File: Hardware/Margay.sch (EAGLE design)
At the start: 70 parts, among them IC1 ATMEGA644M, J1 CONN_42.54_SCREW, J2 CONN_6SCREW_2.54, Q1 FDN360P, Q2 DMG3404, Q3 2N7002, Q4 FDN360P, Q6 FDN360P, U2 FT231X-Q

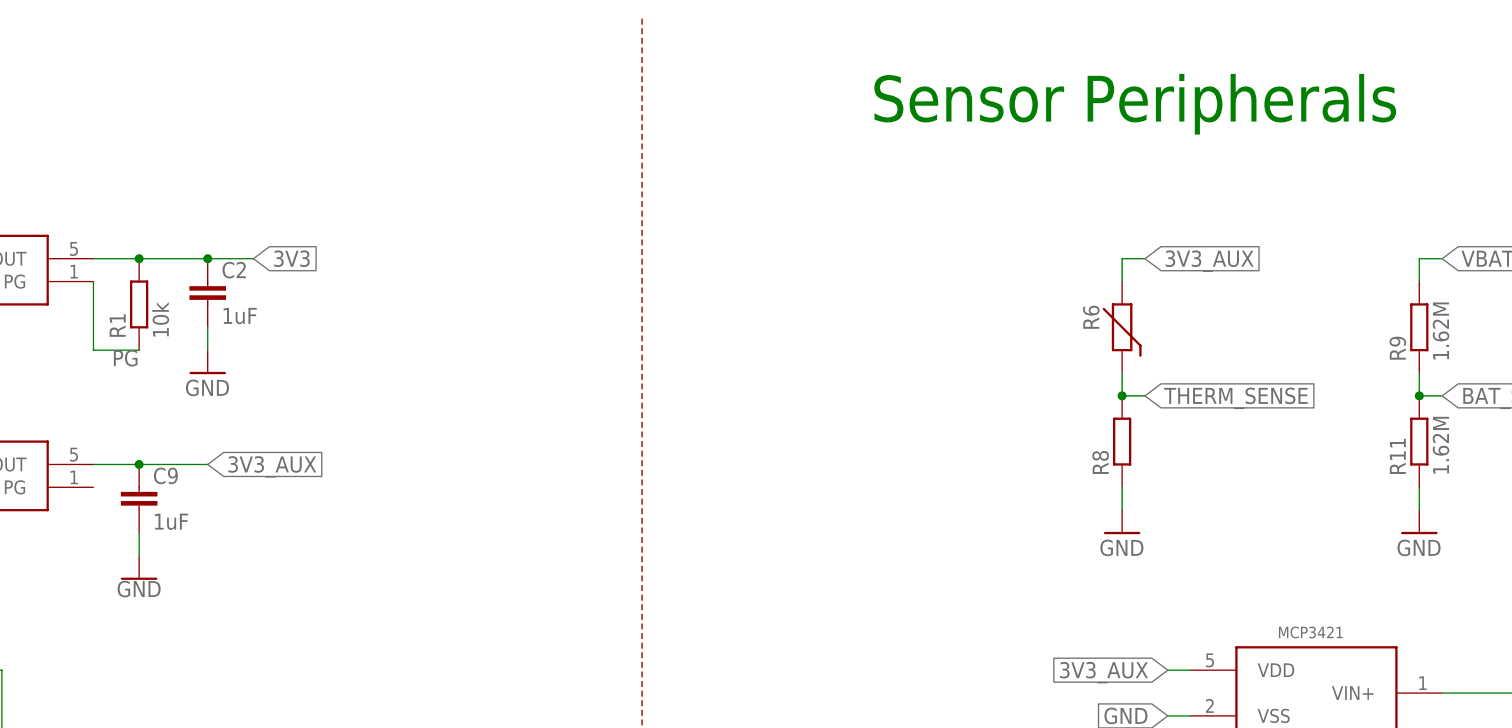
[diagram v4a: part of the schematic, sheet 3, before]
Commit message: First round of v2 updates to schematic
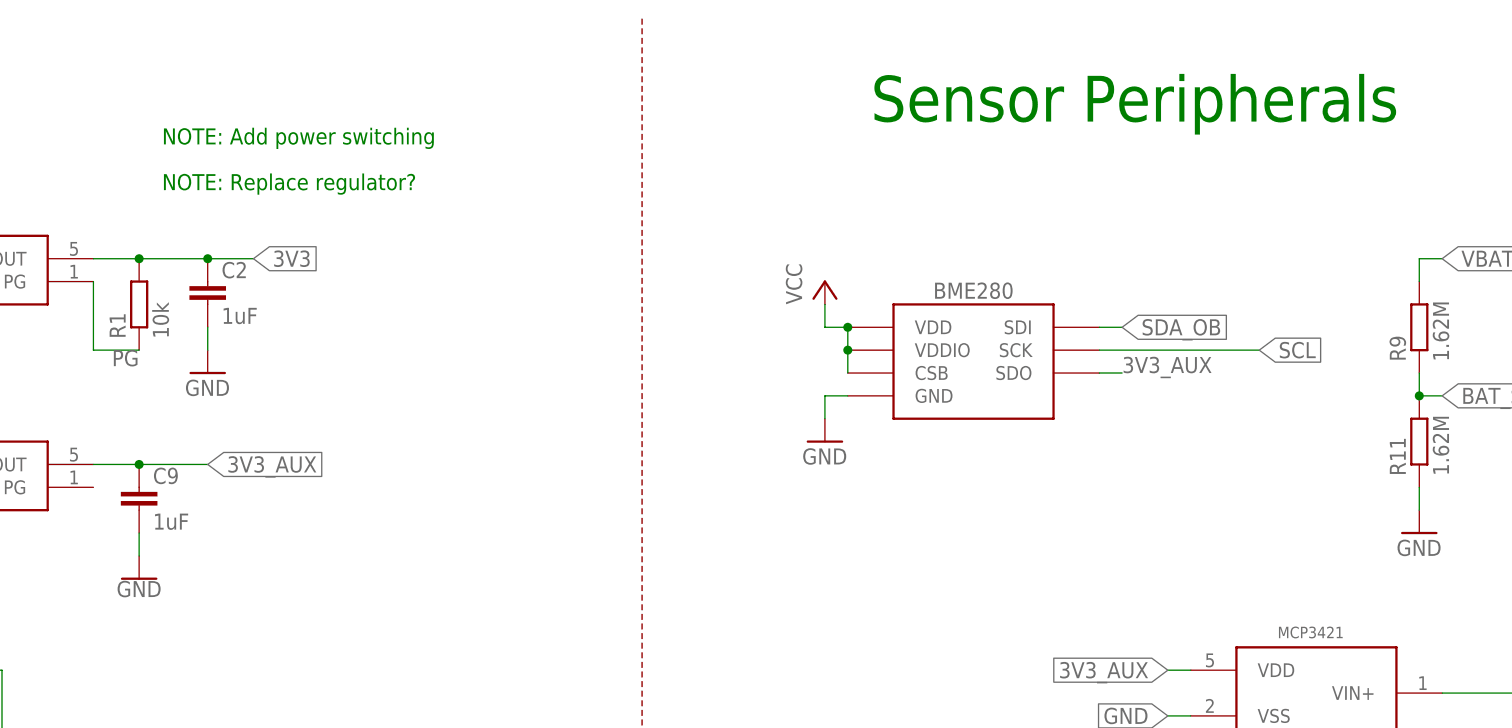
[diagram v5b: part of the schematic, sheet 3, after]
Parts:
- removed R6: (no value), bschulz:THERMISTOR10K
- removed R8: (no value), bschulz_passives:R-EU_P10KR0603
- added R18, R19: 4.7k, bschulz_passives:R-EU_R0402
- added U$12: BME280, bschulz:BME280
- C1, C14, C17, C3, C4, C6, C7, C8: device bschulz_passives:C-EU0.1UFC0603 -> bschulz_passives:C-EU0.1UFC0402
- C21: device bschulz_passives:C-EU1UFC0603 -> bschulz_passives:C-EU0.1UFC0402
- R13, R3: device bschulz:R-EU_10KR0603 -> bschulz_passives:R-EU_10KR0402
- R15: device bschulz_passives:R-EU_10KR0603 -> bschulz_passives:R-EU_R0402
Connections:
- new net ADC_EXT: IC1.(PCINT3/ADC3)PA3, J2.5
- new net RX_EXT: IC1.(PCINT26/INT0)PD2, J2.4
- new net TX_EXT: IC1.(PCINT27/INT1)PD3, J2.3
- net 3V3_AUX: now also R18.2, R19.2, U$12.CSB, U$12.SDO, U$12.VDD, U$12.VDDIO; no longer R6.1
- net EXT_INT: no longer IC1.(PCINT27/INT1)PD3
- net GND: now also U$12.GND; no longer R8.1
- net LOG_INT: now also IC1.(PCINT4/ADC4)PA4; no longer IC1.(PCINT10/INT2/AIN0)PB2
- net MISO: no longer J2.4
- net MOSI_BUF: no longer J2.3
- net RTC_INT: now also IC1.(PCINT10/INT2/AIN0)PB2; no longer IC1.(PCINT26/INT0)PD2
- net SCK_BUF: no longer J2.5
- net SCL: now also R19.1, U$12.SCK
- net SDA: now also R18.1
- net SDA_OB: now also U$12.SDI
- net THERM_SENSE: no longer R6.2, R8.2
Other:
- note added: "Ext Int0"
- note added: "Ext Int1"
- note added: "I2C pullup to switched 3v3"
- note added: "NOTE: Add power switching"
- note added: "NOTE: Add voltage divider to ADC Ext??"
- note added: "NOTE: Check orientation of TX and RX"
- note added: "NOTE: Fix connector orientation on PCB!"
- note added: "NOTE: REDUCE RESISTOR SIZE"
- note added: "NOTE: Replace regulator?"
- note removed: "Jump auxillary power rails together, reduces brownout protection"

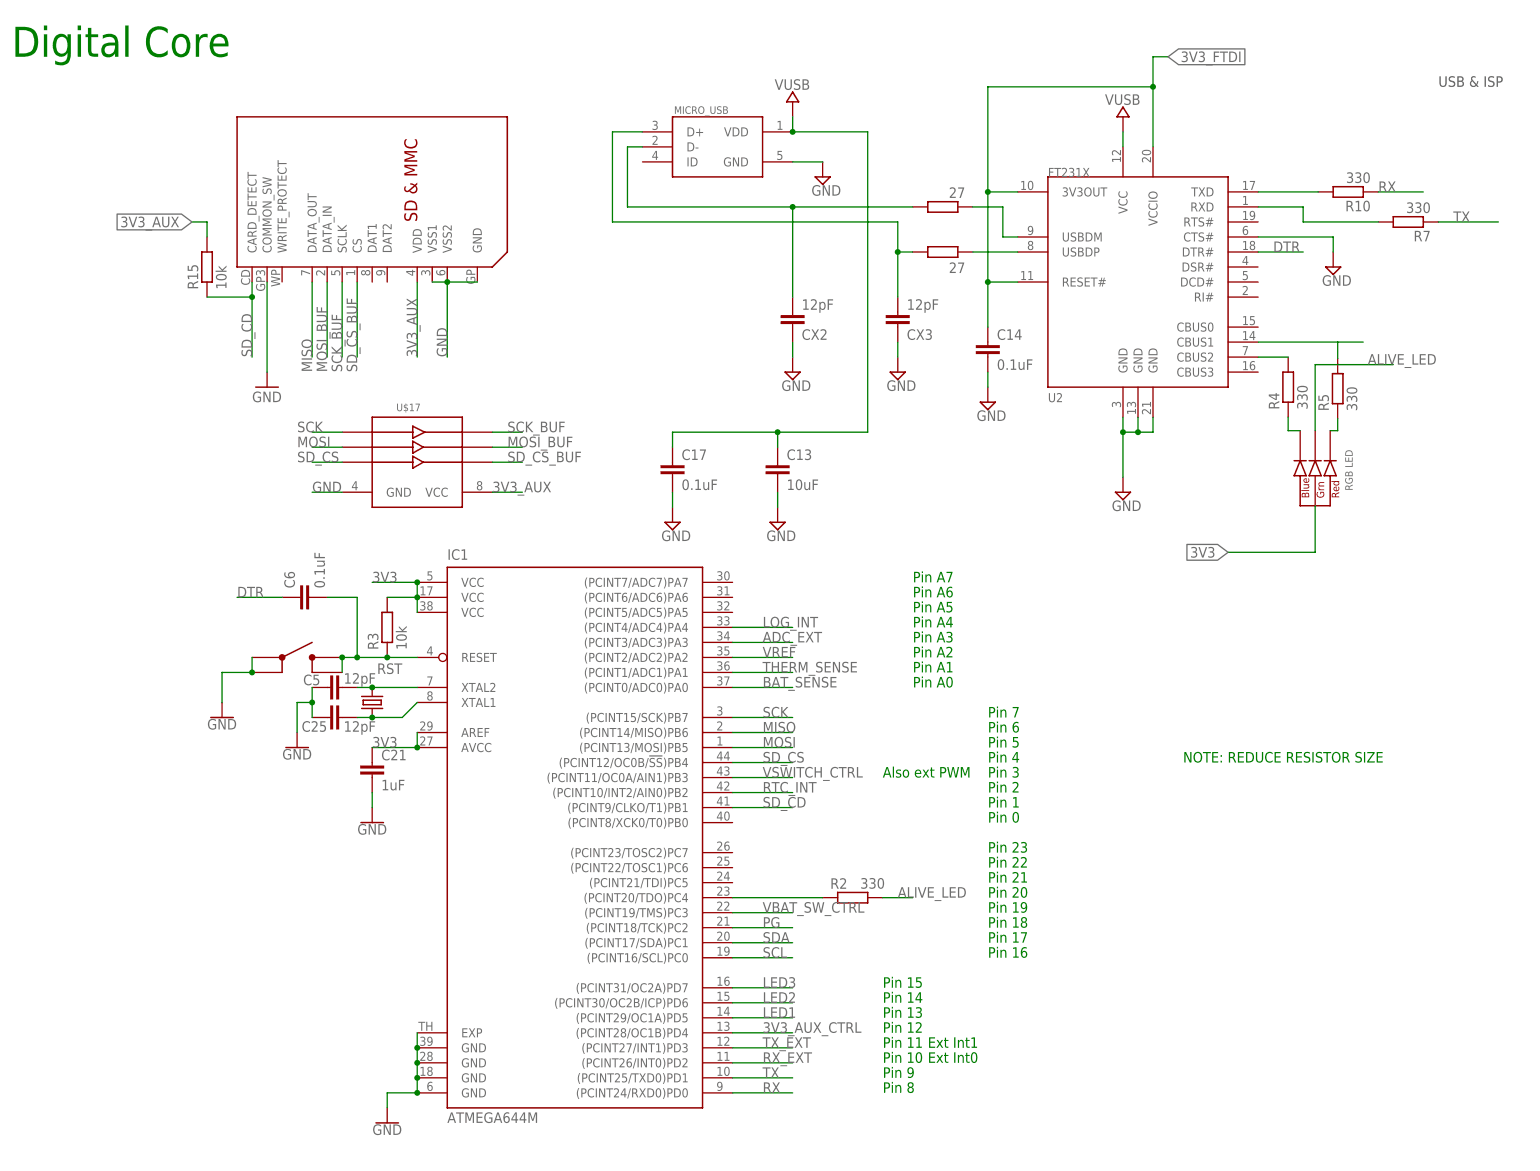
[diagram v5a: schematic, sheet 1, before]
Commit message: Revised schematic for Margay v2, added circuit simulations
Will remove some simulations later, still need to do much layout and placement, as well as verify the schematic
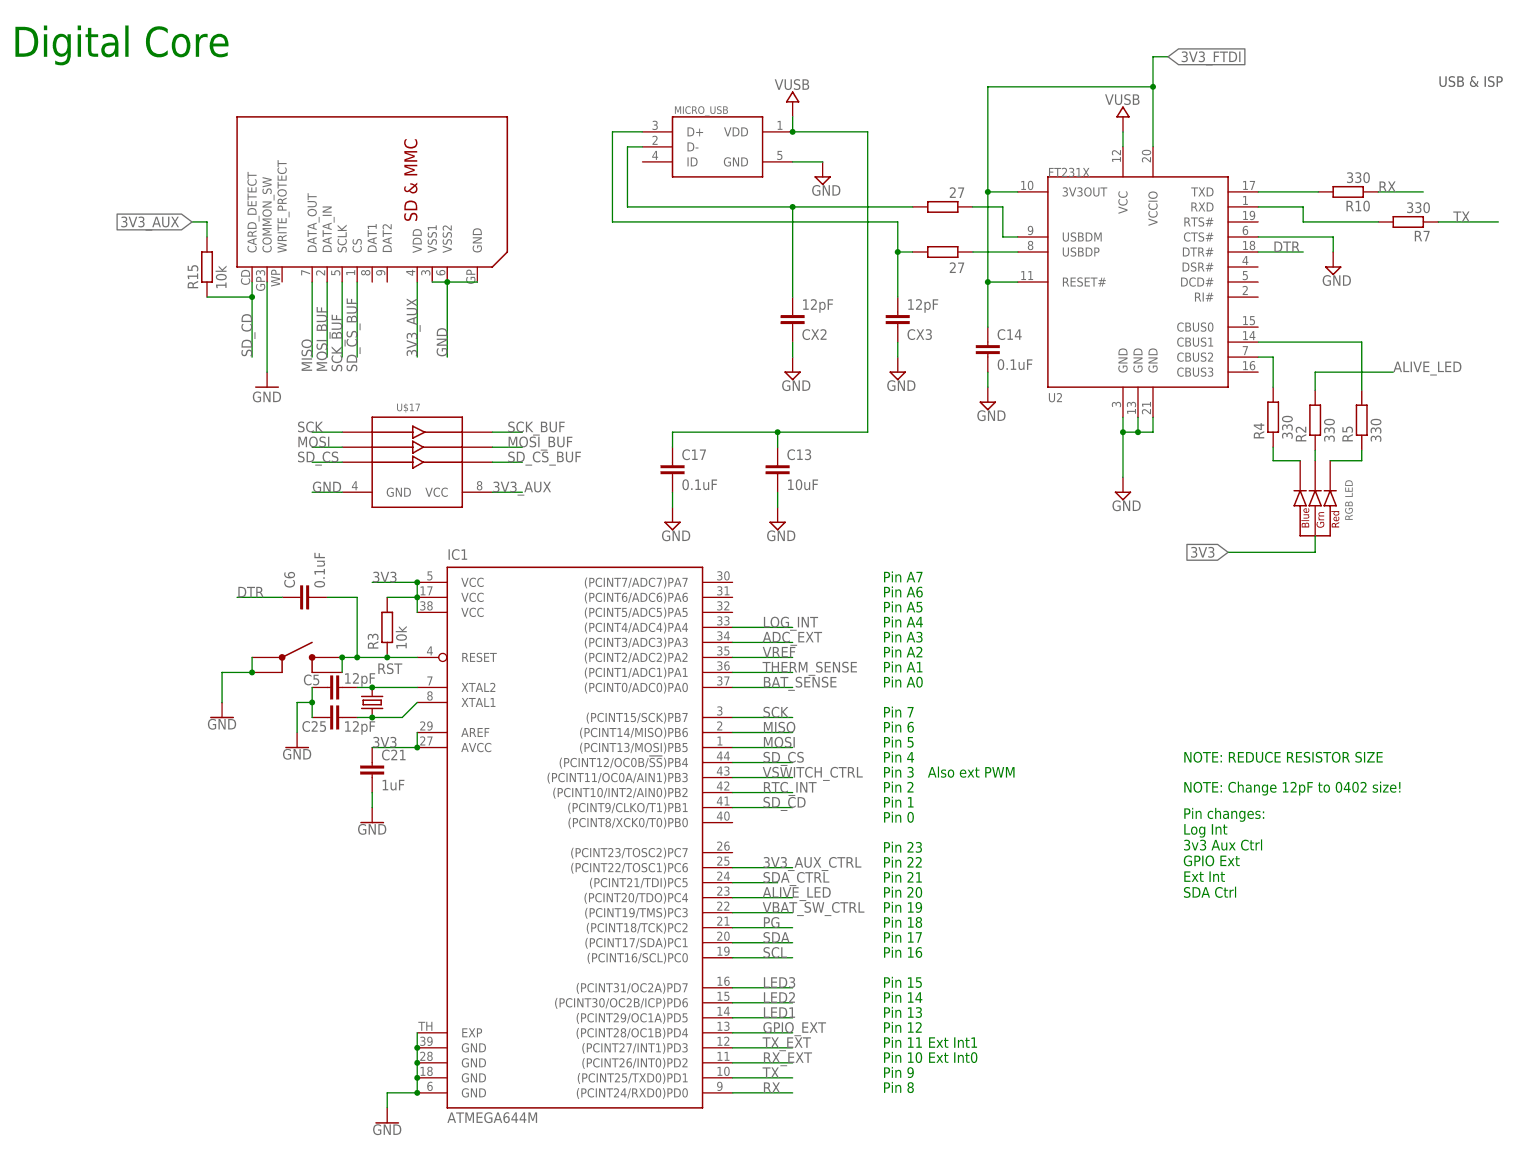
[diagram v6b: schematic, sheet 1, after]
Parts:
- removed Q6: FDN360P, bschulz:MOSFET_PCH-FDN360P
- removed U$10: TPS79733, bschulz:TPS79733
- removed U$11: MIC842H, bschulz:MIC842H
- added C10, C11: 0.1uF, bschulz_passives:C-EU0.1UFC0402
- added C12: 1uF, bschulz_passives:C-EU1UFC0603
- added U$18: TPS2105, bschulz:TPS2105
- added U1: TPS7A0533DBV, bschulz:TPS7A0533DBV
- C25, C5: device bschulz_passives:C-EUC0603 -> bschulz_passives:C-EU12PFC0402
- C7: value 0.1uF -> 1uF; device bschulz_passives:C-EU0.1UFC0402 -> bschulz_passives:C-EU1UFC0603
- C9: value 1uF -> 10uF; device bschulz_passives:C-EU1UFC0603 -> bschulz_passives:C-EU10UFC0805
- CX2, CX3: device bschulz_passives:C-EU12PFC0603 -> bschulz_passives:C-EU12PFC0402
- D+, D-: device bschulz_passives:R-EU_27R0603 -> bschulz_passives:R-EU_27R0402
- R1: device bschulz_passives:R-EU_10KR0603 -> bschulz_passives:R-EU_10KR0402
- R10, R4, R5, R7: device bschulz_passives:R-EU_330R0603 -> bschulz_passives:R-EU_330R0402
- R12: device bschulz_passives:R-EU_10KR0603 -> bschulz_passives:R-EU_P10KR0603
- R14, R23, R24: device bschulz:R-EU_330R0603 -> bschulz_passives:R-EU_330R0402
- R17: device bschulz_passives:R-EU_10KR0603 -> bschulz_passives:R-EU_330R0402
- R18, R19: device bschulz_passives:R-EU_R0402 -> bschulz_passives:R-EU_4.7KR0402
- R2: device bschulz:R-EU_330R0603 -> bschulz_passives:R-EU_330R0402; DIGIKEY (none) -> 311-330HRCT-ND; MPN (none) -> RC0603FR-07330RL
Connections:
- removed net EXT_INT: J2.6
- removed net N$4 (its old number): Q6.G, U$11.OUT
- new net GPIO_EXT: IC1.(PCINT28/OC1B)PD4, J2.6
- new net SDA_CTRL: IC1.(PCINT21/TDI)PC5, U$13.S
- net 3V3_AUX: now also U1.VOUT; no longer U$10.VOUT
- net 3V3_AUX_CTRL: now also IC1.(PCINT22/TOSC1)PC6, U1.EN; no longer IC1.(PCINT28/OC1B)PD4, U$13.S
- net ALIVE_LED: no longer U$16.GREEN_CATH
- net GND: now also C10.2, C11.2, C12.2, U$18.GND, U1.GND; no longer U$10.GND, U$11.GND
- net N$1: now also U$16.GREEN_CATH; no longer IC1.(PCINT20/TDO)PC4
- net VBAT+: now also C10.1, U$18.IN1; no longer Q6.S, U$11.VDD
- net VBAT_SW: now also C12.1, U$18.OUT, U1.VIN; no longer Q6.D, U$10.VIN
- net VBAT_SW_CTRL: now also U$18.EN; no longer U$11.INP
- net VUSB: now also C11.1, U$18.IN2
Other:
- note added: "NOTE: Add enable line connection??"
- note added: "NOTE: Add silkscreen note!"
- note added: "NOTE: Change 12pF to 0402 size!"
- note added: "NOTE: Reduce resistance?? Add capacitor in parellel"
- note added: "Pin changes: Log Int 3v3 Aux Ctrl GPIO Ext Ext Int SDA Ctrl"
- note removed: "NOTE: Replace regulator?"
- moved on the sheet: C9, R2, R4, R5

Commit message: Begining of v2 layout
Power section and severl problematic signals taken care of, still need to add BME280 and fix header connections
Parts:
- R17: device bschulz_passives:R-EU_330R0402 -> bschulz_passives:R-EU_10KR0402
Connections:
- net ALIVE_LED: now also IC1.(PCINT20/TDO)PC4
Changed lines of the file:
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@@
 <?xml version="1.0" encoding="utf-8"?>
 <!DOCTYPE eagle SYSTEM "eagle.dtd">
-<eagle version="9.0.1">
+<eagle version="9.1.3">
 <drawing>
 <settings>
@@
 <part name="Q4" library="bschulz" deviceset="MOSFET_PCH" device="-FDN360P" value="FDN360P"/>
 <part name="R16" library="bschulz_passives" deviceset="R-EU_" device="R0603" technology="180K" value="180k"/>
-<part name="R17" library="bschulz_passives" deviceset="R-EU_" device="R0402" technology="330" value="10k"/>
+<part name="R17" library="bschulz_passives" deviceset="R-EU_" device="R0402" technology="10K" value="10k"/>
 <part name="GND11" library="SparkFun-PowerSymbols" library_urn="urn:adsk.eagle:library:530" deviceset="GND" device=""/>
 <part name="C7" library="bschulz_passives" deviceset="C-EU" device="C0603" technology="1UF" value="1uF"/>
@@
 <wire x1="132.08" y1="58.42" x2="142.24" y2="58.42" width="0.1524" layer="91"/>
 <label x="137.16" y="58.42" size="1.778" layer="95"/>
-</segment>
-<segment>
+<pinref part="IC1" gate="G$1" pin="(PCINT20/TDO)PC4"/>
+</segment>
+<segment>

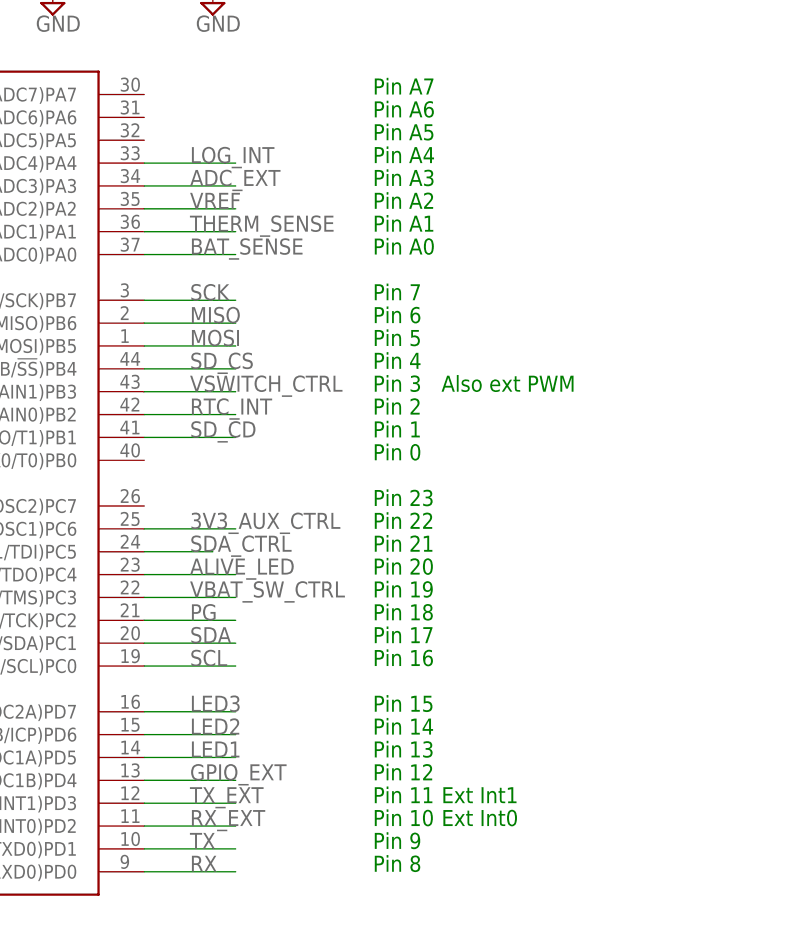
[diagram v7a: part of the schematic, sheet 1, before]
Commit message: Main v2 layout complete, needs review minor cleanup
Main layout is completed, needs verification and review for any traces which need to be cleaned up. Double check power on schematic!
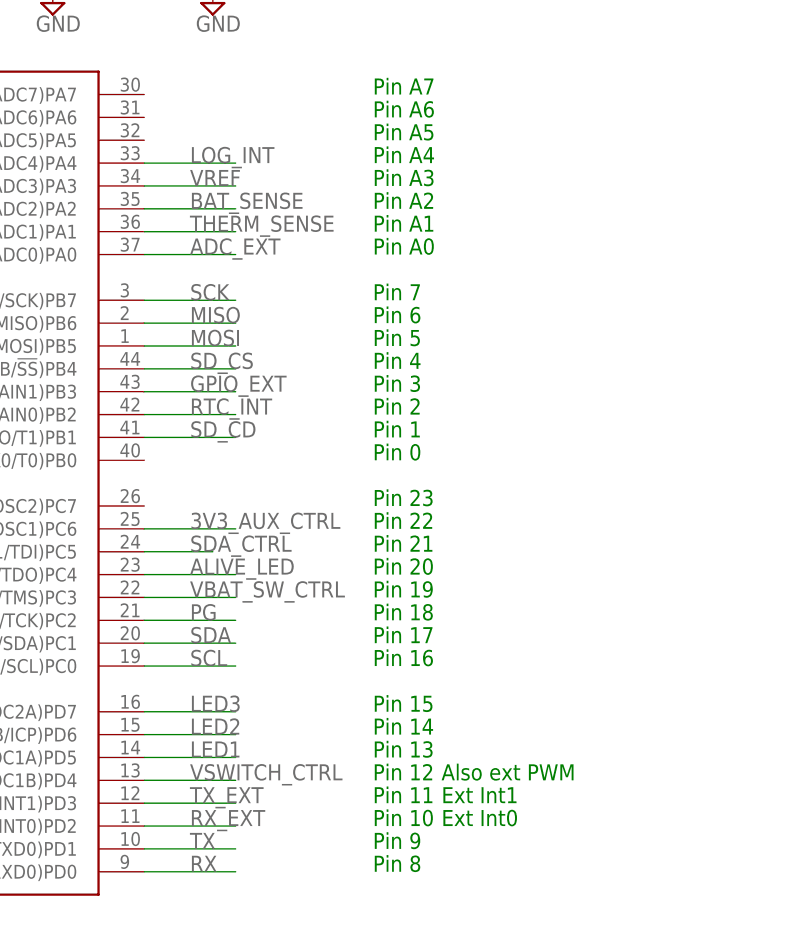
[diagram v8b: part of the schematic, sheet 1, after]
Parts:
- removed C12: 1uF, bschulz_passives:C-EU1UFC0603
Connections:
- net ADC_EXT: now also IC1.(PCINT0/ADC0)PA0; no longer IC1.(PCINT3/ADC3)PA3
- net BAT_SENSE: now also IC1.(PCINT2/ADC2)PA2; no longer IC1.(PCINT0/ADC0)PA0
- net GND: no longer C12.2
- net GPIO_EXT: now also IC1.(PCINT11/OC0A/AIN1)PB3; no longer IC1.(PCINT28/OC1B)PD4
- net VBAT_SW: no longer C12.1
- net VREF: now also IC1.(PCINT3/ADC3)PA3; no longer IC1.(PCINT2/ADC2)PA2
- net VSWITCH_CTRL: now also IC1.(PCINT28/OC1B)PD4; no longer IC1.(PCINT11/OC0A/AIN1)PB3
